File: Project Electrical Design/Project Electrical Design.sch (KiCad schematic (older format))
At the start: 18 parts, among them SW1 SW_Push_LED, SW2 SW_Push_LED, SW3 SW_Push_LED, SW4 SW_Push_LED

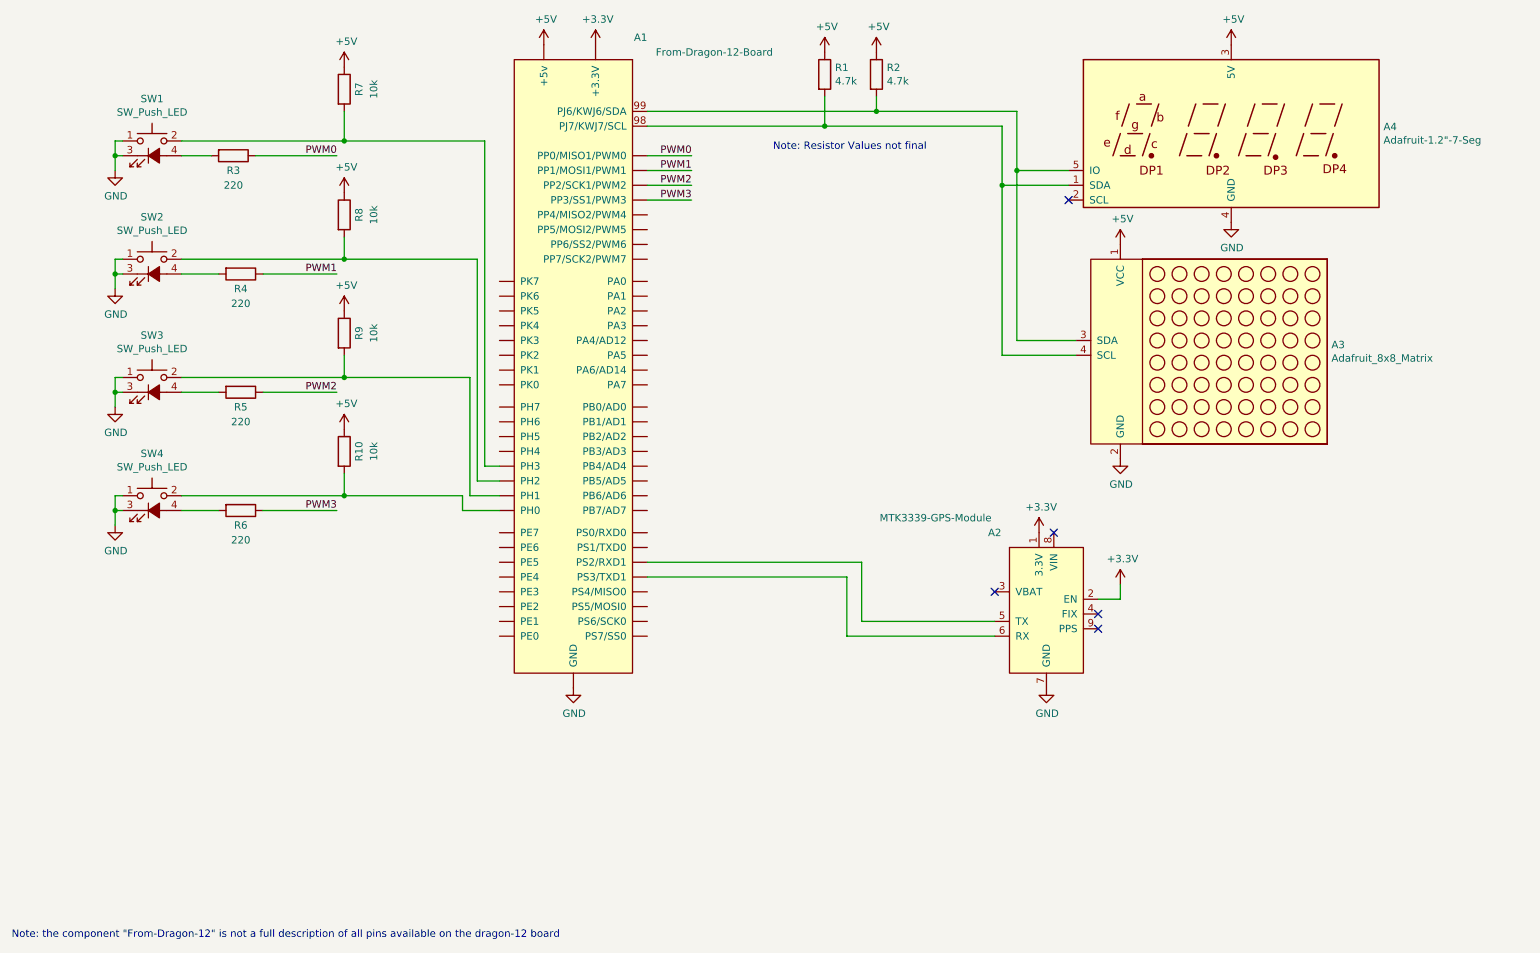
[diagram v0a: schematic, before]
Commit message: Added figures, demonstration video, and modified electrical schematic.
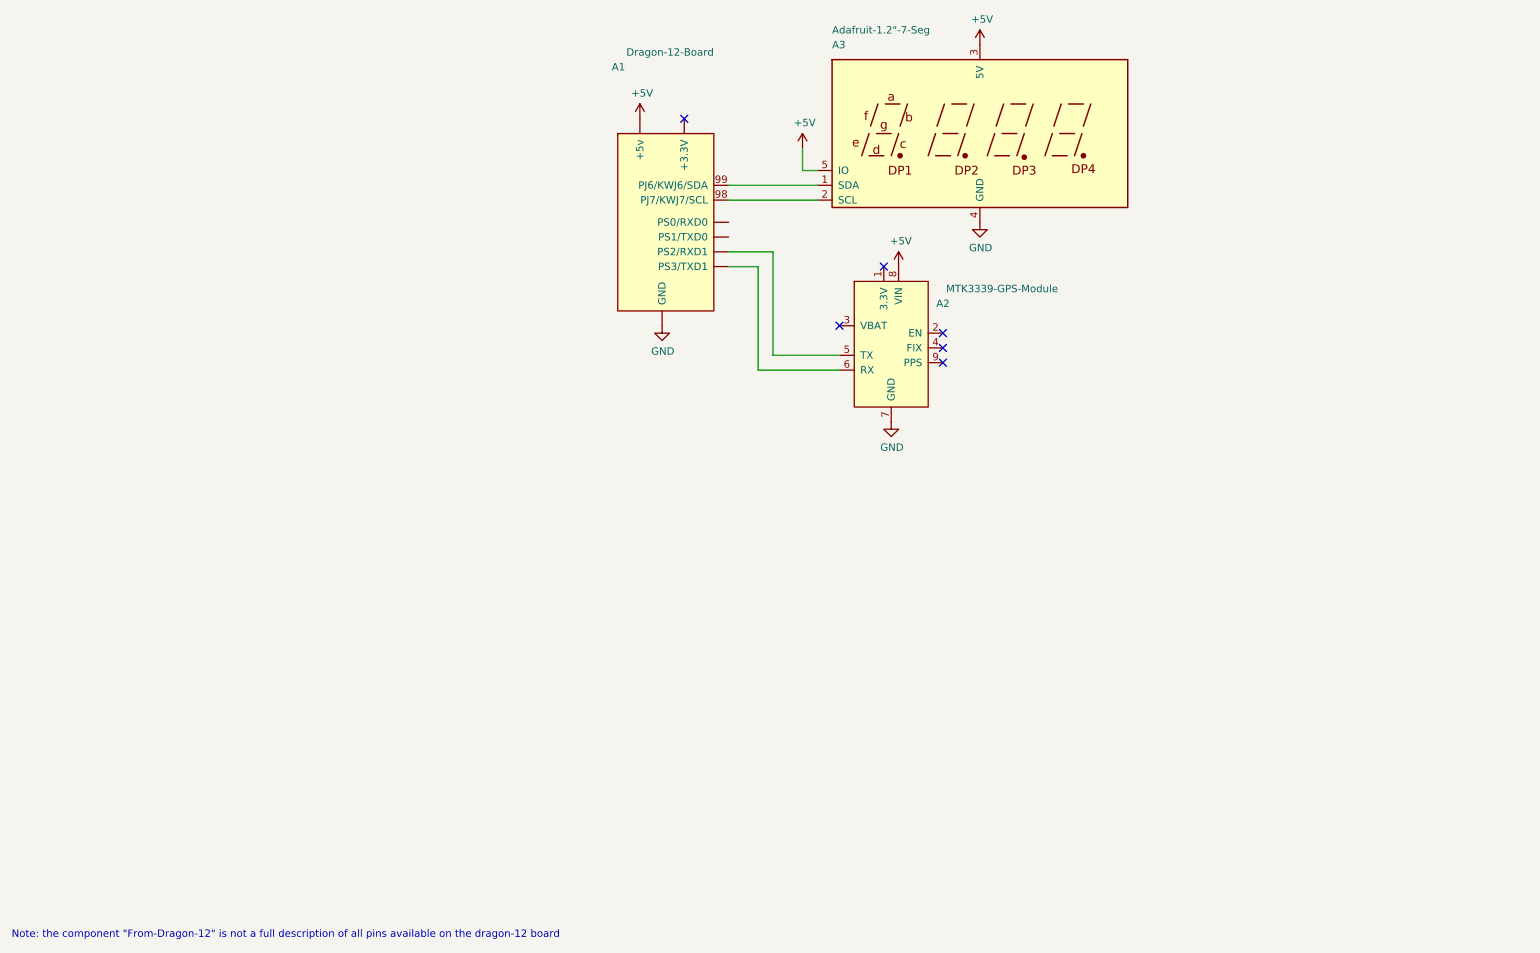
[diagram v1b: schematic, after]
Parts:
- removed A1: From-Dragon-12-Board, symbol CustomParts:From-Dragon-12-Board
- removed A3: Adafruit_8x8_Matrix, symbol CustomParts:Adafruit_8x8_Matrix
- removed A4: Adafruit-1.2\"-7-Seg, symbol CustomParts:Adafruit-1.2"-7-Seg
- removed R1, R2: 4.7k, symbol Device:R
- removed R10, R7, R8, R9: 10k, symbol Device:R
- removed R3, R4, R5, R6: 220, symbol Device:R
- removed SW1, SW2, SW3, SW4: SW_Push_LED, symbol Switch:SW_Push_LED
- added A1: Dragon-12-Board, symbol CustomParts:Dragon-12-Board
- added A3: Adafruit-1.2\"-7-Seg, symbol CustomParts:Adafruit-1.2"-7-Seg
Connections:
- net +5V: now also A2.8 (VIN), A1.~ (PS3/TXD1), A3.3 (5V), A3.5 (IO)
- net GND: now also A1.~ (PS3/TXD1), A3.4 (GND)
- net at A2.5 (TX): now also A1.~ (PS3/TXD1)
- net at A2.6 (RX): now also A1.~ (PS3/TXD1)
- net +3V3: no longer names the net of A2.1 (3.3V)
- net +3V3: no longer A2.2 (EN)
- new net: A1.99 (PJ6/KWJ6/SDA), A3.1 (SDA)
- new net: A1.98 (PJ7/KWJ7/SCL), A3.2 (SCL)
- no-connect marks 5 -> 6
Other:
- note removed: "Note: Resistor Values not final\n\n"
